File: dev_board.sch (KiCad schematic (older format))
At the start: 13 parts, among them J1 USB_B_Micro, J2 ARJ-169, J3 Conn_02x10_Odd_Even, J4 Conn_02x10_Odd_Even, SW1 SW_Push

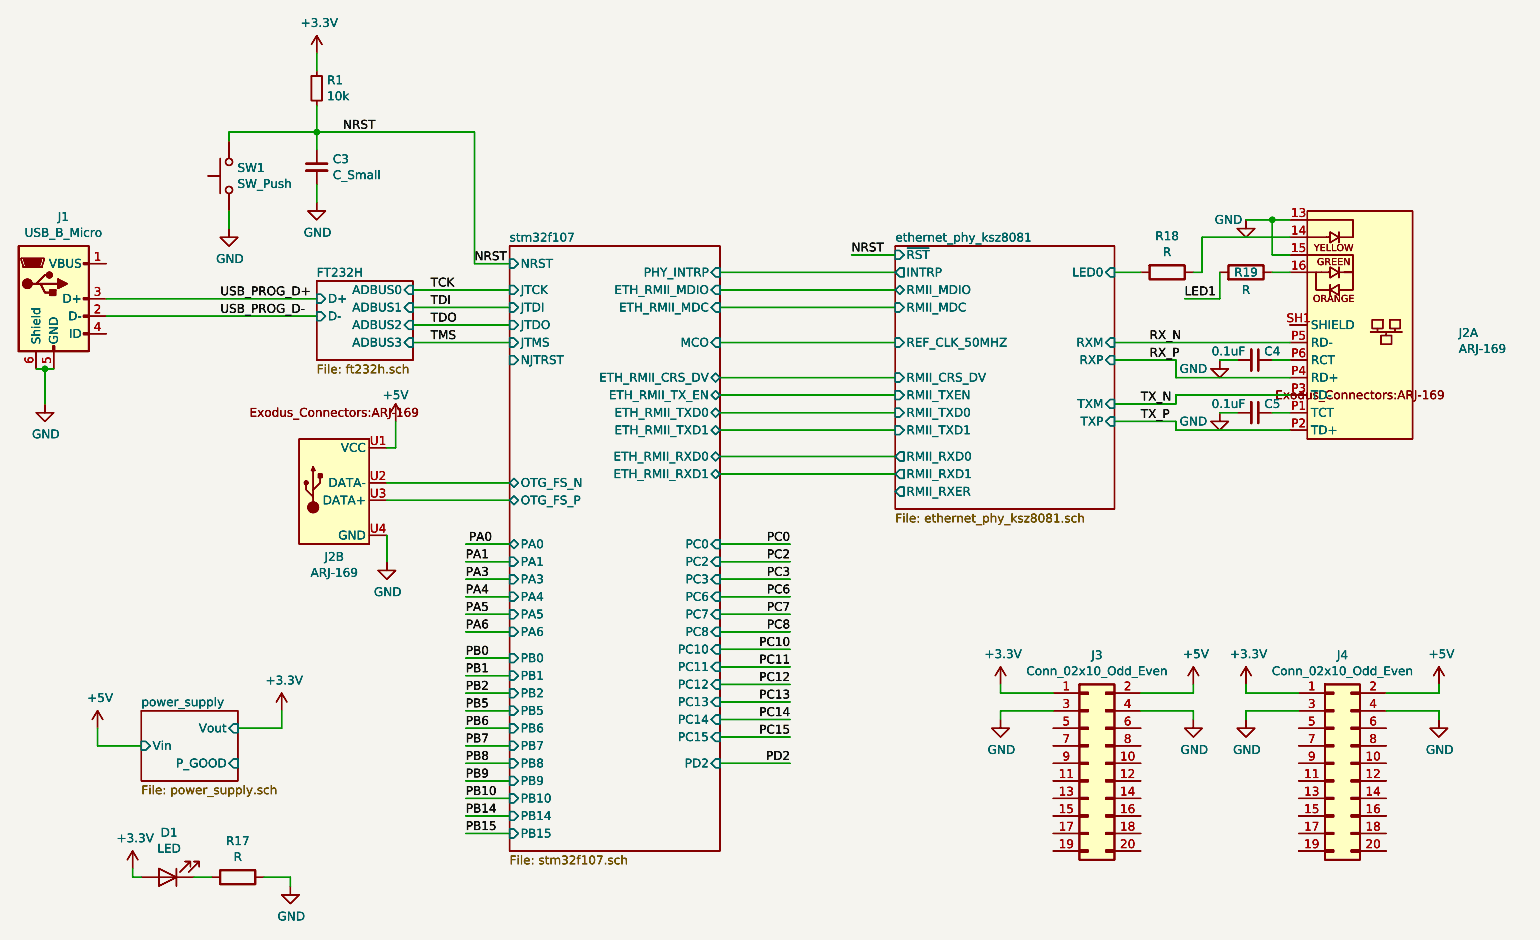
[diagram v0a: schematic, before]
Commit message: redirected 3D models for custom footprints on PCB
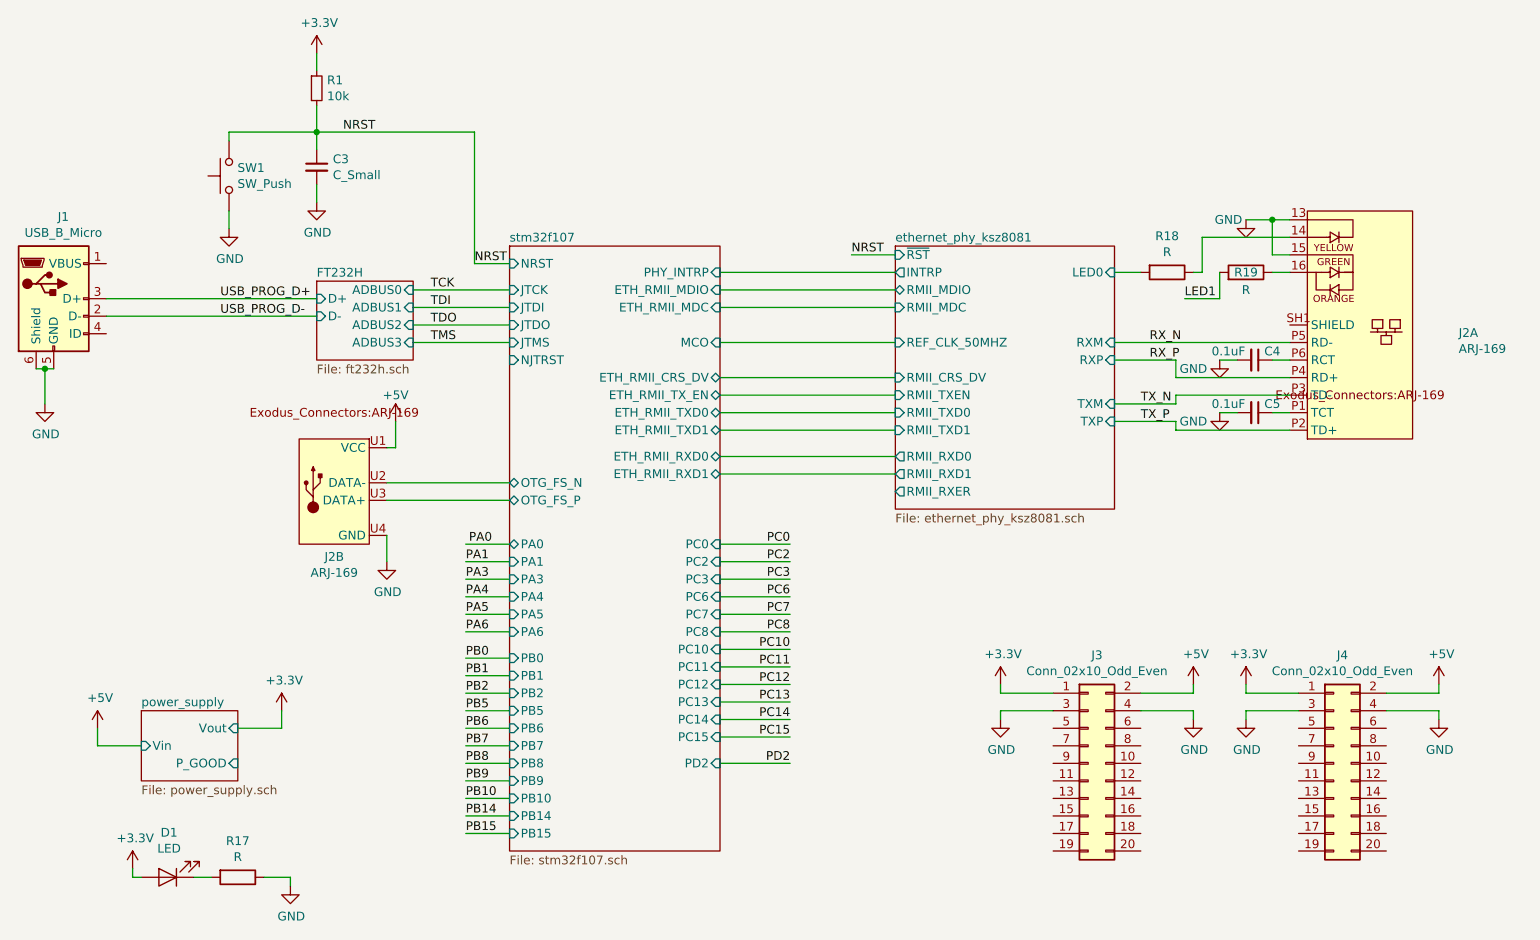
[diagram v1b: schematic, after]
